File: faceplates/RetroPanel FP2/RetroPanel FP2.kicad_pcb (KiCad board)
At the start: 2 copper layers, 101.5 x 26 mm, 13 parts, among them M1 Mounting_Pin, M10 Mounting_Pad, M2 Mounting_Pin, M3 Mounting_Pin, M4 Mounting_Pin, M5 Mounting_Pad, M6 Mounting_Pad, M7 Mounting_Pad, M8 Mounting_Pad, M9 Mounting_Pad

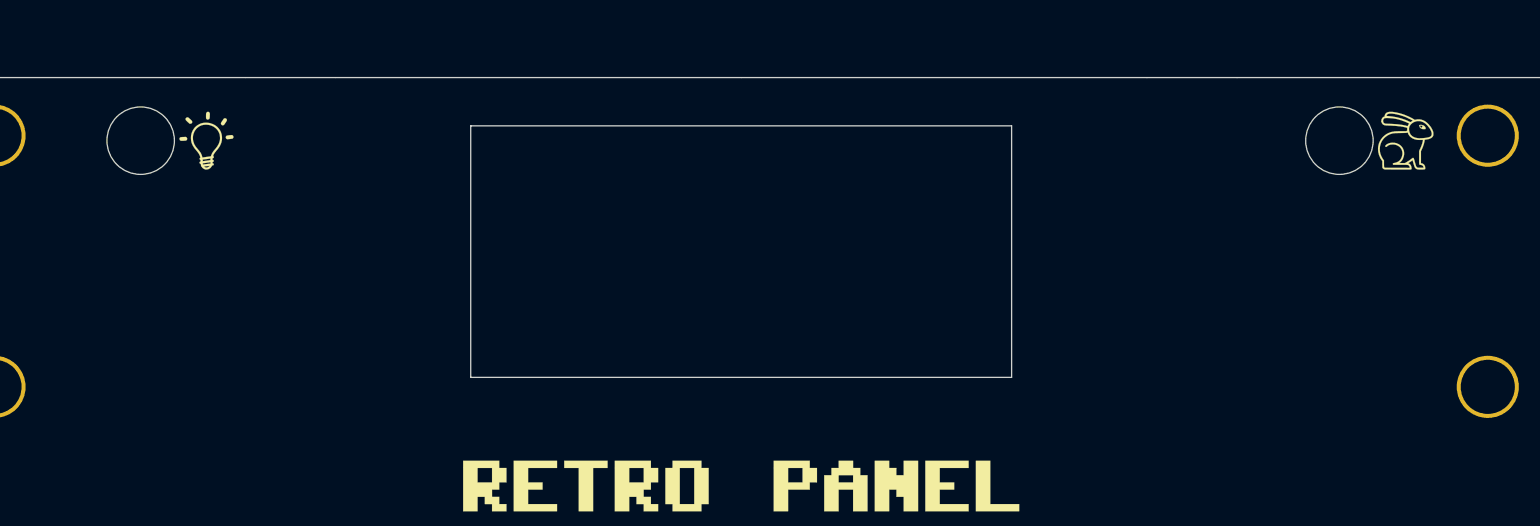
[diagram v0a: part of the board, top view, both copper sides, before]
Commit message: Faceplate tweaks (non-visible)
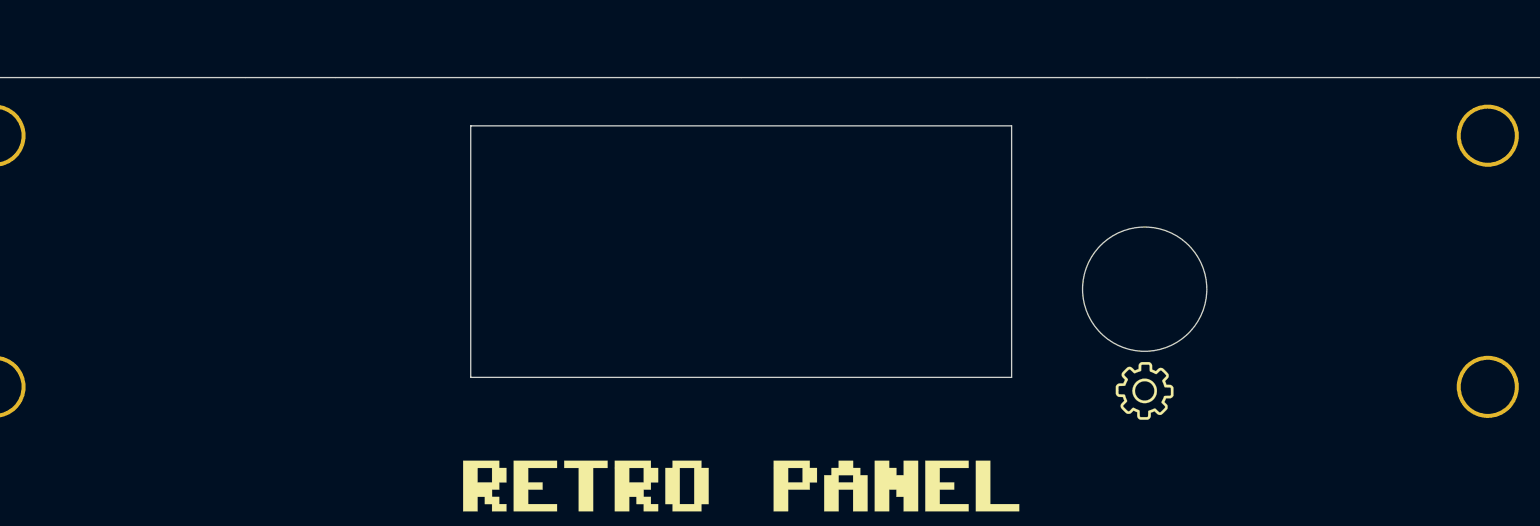
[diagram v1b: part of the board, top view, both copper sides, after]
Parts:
- removed the G*** at (120.6, 82.9)
- removed the G*** at (188.2, 82.9)
- added G***: LOGO, RetroPanel:icon_extra, F.Cu at (173.5, 97.0)
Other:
- outline, holes or cut-outs redrawn

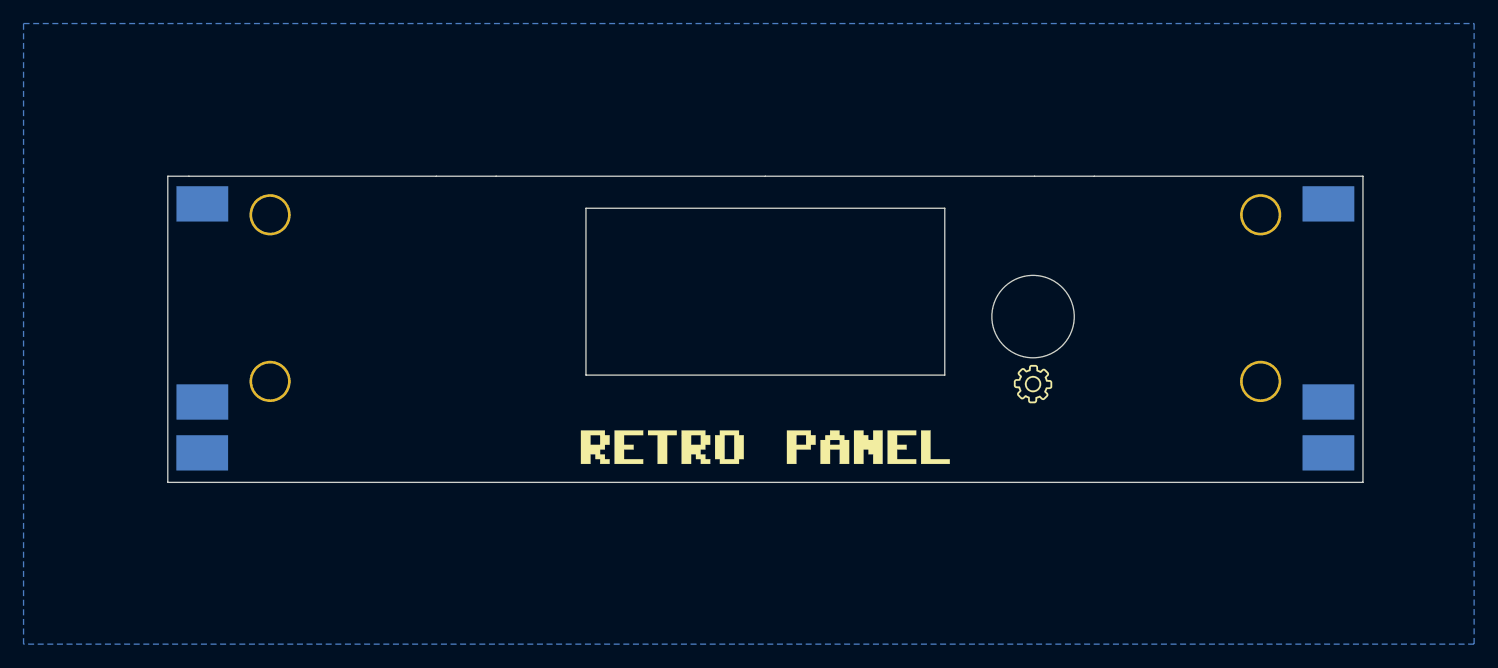
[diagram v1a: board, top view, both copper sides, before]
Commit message: Shorten lower lip
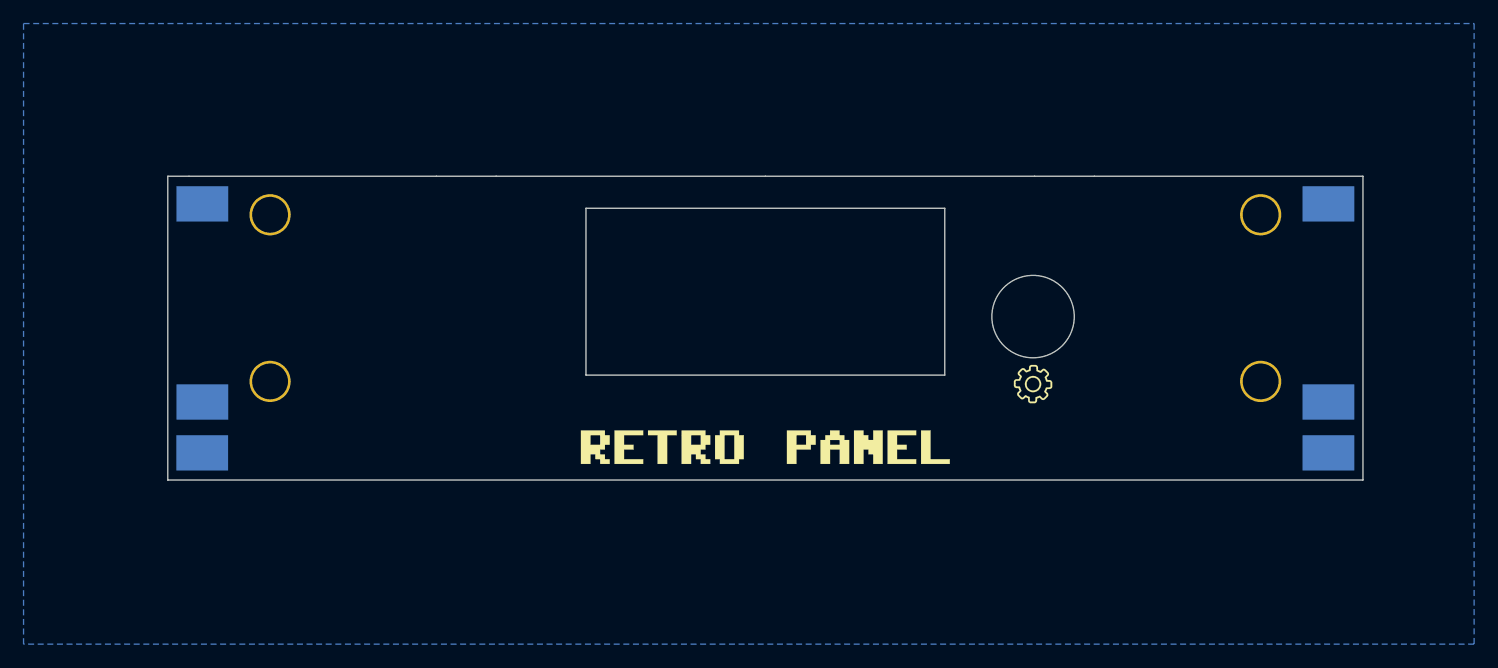
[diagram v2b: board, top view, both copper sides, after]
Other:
- board size 101.5 x 26 mm -> 101.5 x 25.8 mm
- board text added: "3.5" RetroPanel Faceplate FP2 (rev. B) github.com/tebl"
- board text removed: "3.5" RetroPanel Faceplate FP2 (rev. A) github.com/tebl"
